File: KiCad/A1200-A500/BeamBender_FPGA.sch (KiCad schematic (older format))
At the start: 2 parts, among them U2 GW1NR-UV9LQ144P

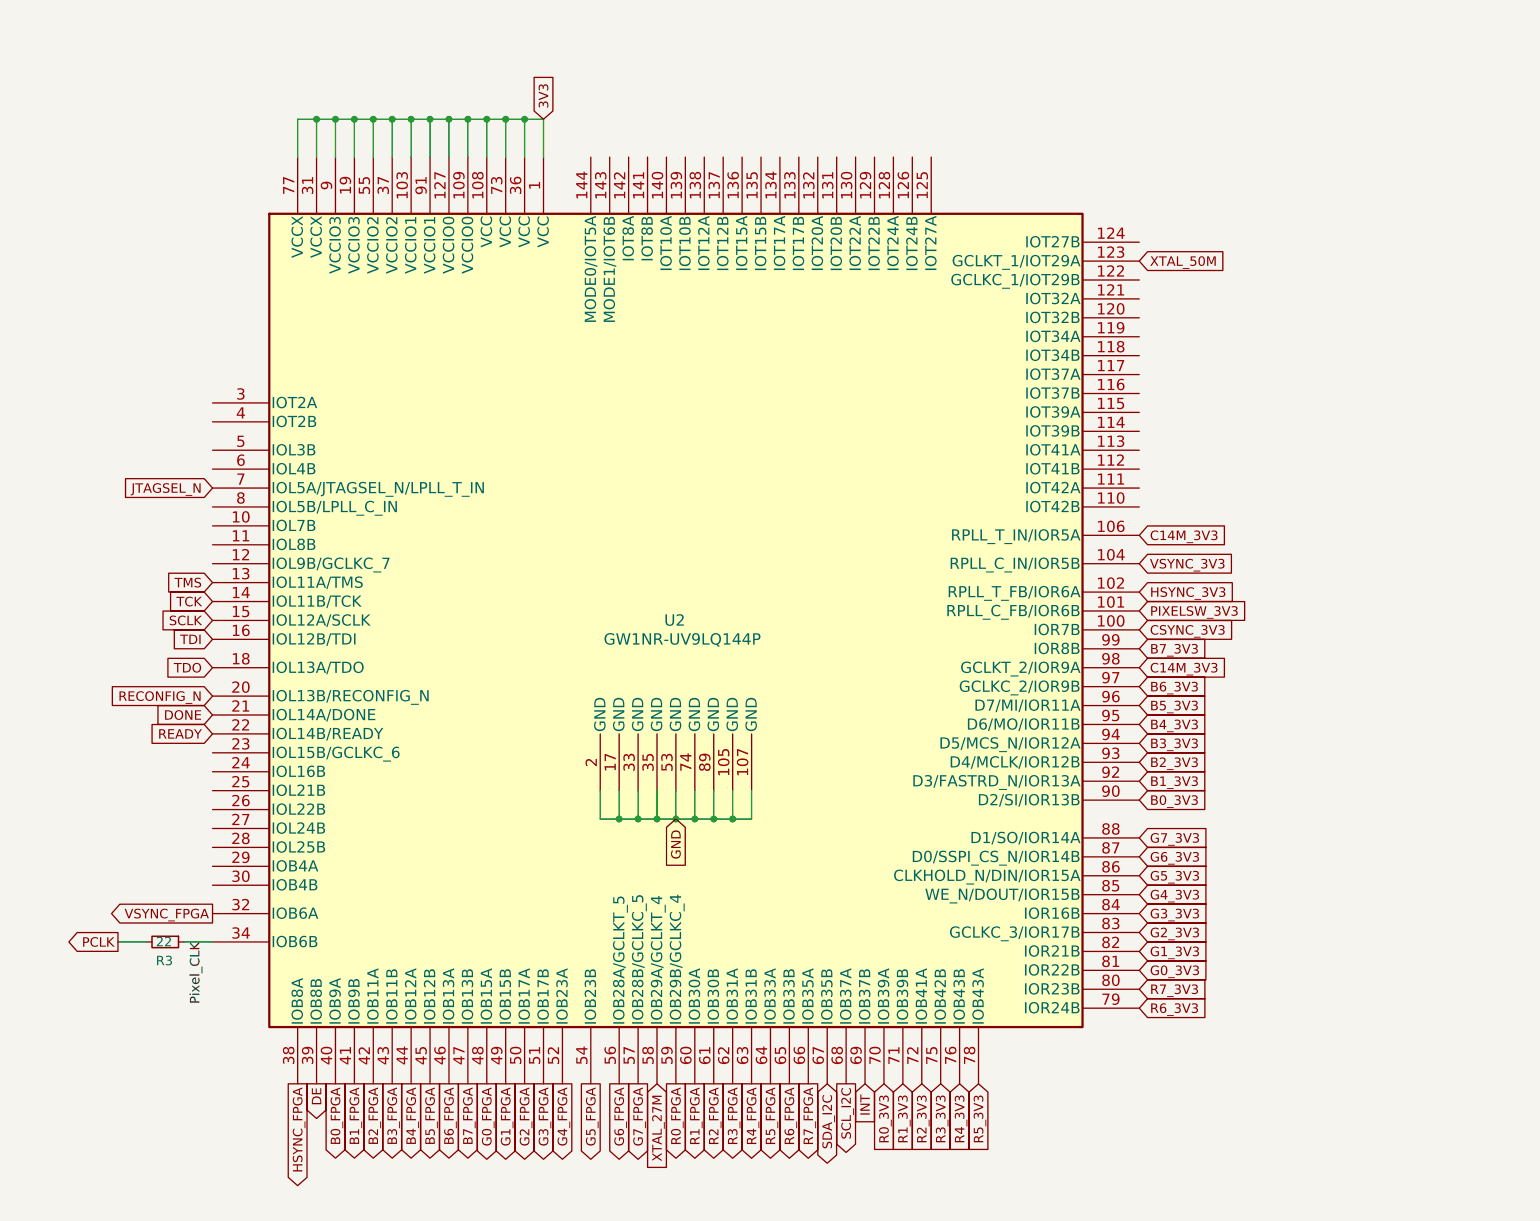
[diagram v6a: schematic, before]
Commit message: Breakout of own symbol for A500 drill-hole and more assignments of FPGA-pins
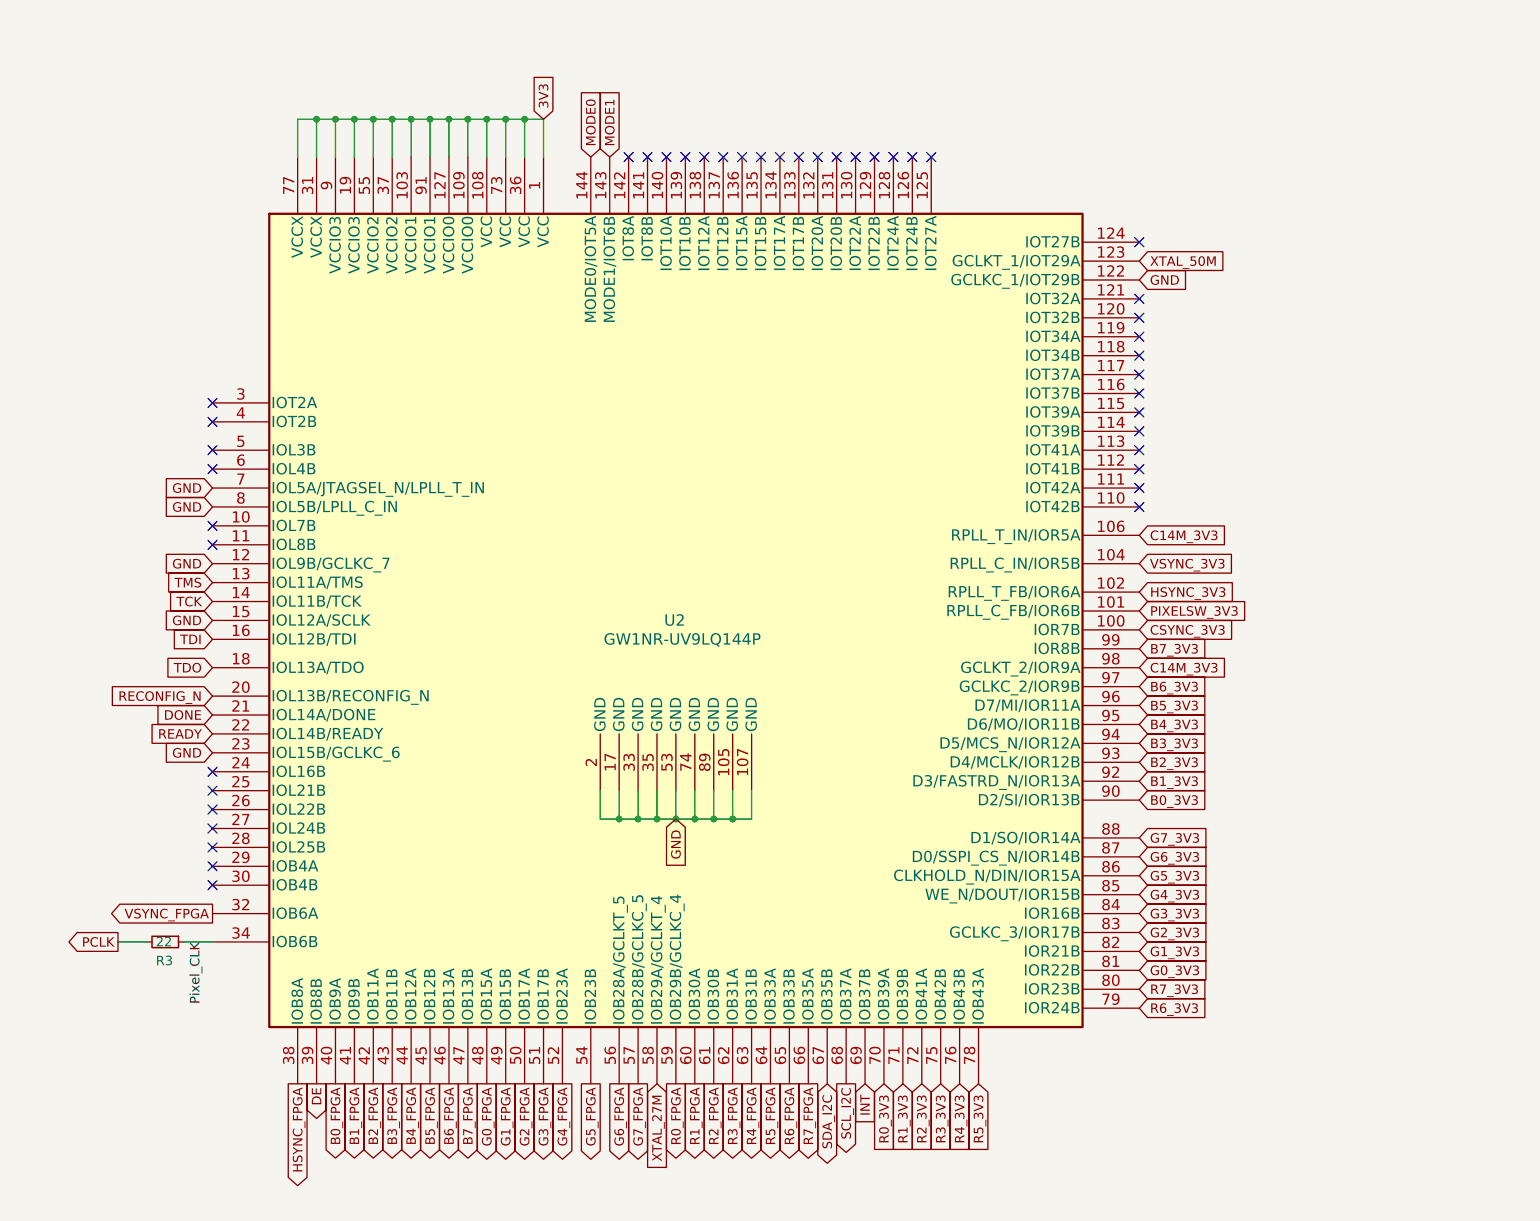
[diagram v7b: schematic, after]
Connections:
- net JTAGSEL_N is gone; now on net GND: U2.7 (IOL5A/JTAGSEL_N/LPLL_T_IN)
- net SCLK is gone; now on net GND: U2.15 (IOL12A/SCLK)
- net GND: now also U2.12 (IOL9B/GCLKC_7), U2.122 (GCLKC_1/IOT29B), U2.23 (IOL15B/GCLKC_6), U2.8 (IOL5B/LPLL_C_IN)
- net MODE1: now reaches U2.143 (MODE1/IOT6B)
- net MODE0: now reaches U2.144 (MODE0/IOT5A)
- no-connect marks 0 -> 43
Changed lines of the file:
@@
 Text GLabel 1600 3600 0    50   Input ~ 0
 TCK
-Text GLabel 1600 3700 0    50   Input ~ 0
-SCLK
 Text GLabel 1600 3800 0    50   Input ~ 0
 TDI
@@
 Text GLabel 1100 5400 0    50   Output ~ 0
 PCLK
-Text GLabel 1600 3000 0    50   Input ~ 0
-JTAGSEL_N
 Text GLabel 6500 3750 2    50   Input ~ 0
 CSYNC_3V3
@@
 Text Label 1550 5400 3    50   ~ 0
 Pixel_CLK
+Text GLabel 3600 1250 1    50   Input ~ 0
+MODE0
+Text GLabel 3700 1250 1    50   Input ~ 0
+MODE1
+Text GLabel 1600 3100 0    50   Input ~ 0
+GND
+Text GLabel 1600 3400 0    50   Input ~ 0
+GND
+Text GLabel 1600 3700 0    50   Input ~ 0
+GND
+Text GLabel 1600 4400 0    50   Input ~ 0
+GND
+Text GLabel 1600 3000 0    50   Input ~ 0
+GND
+NoConn ~ 1600 2550
+NoConn ~ 1600 2650
+NoConn ~ 1600 2800
+NoConn ~ 1600 2900
+NoConn ~ 1600 3200
+NoConn ~ 1600 3300
+NoConn ~ 1600 4500
+NoConn ~ 1600 4600
+NoConn ~ 1600 4700
+NoConn ~ 1600 4800
+NoConn ~ 1600 4900
+NoConn ~ 1600 5000
+NoConn ~ 1600 5100
+NoConn ~ 6500 1700
+NoConn ~ 6500 2000
+NoConn ~ 6500 2100
+NoConn ~ 6500 2200
+NoConn ~ 6500 2300
+NoConn ~ 6500 2400
+NoConn ~ 6500 2500
+NoConn ~ 6500 2600
+NoConn ~ 6500 2700
+NoConn ~ 6500 2800
+NoConn ~ 6500 2900
+NoConn ~ 6500 3000
+NoConn ~ 6500 3100
+NoConn ~ 3800 1250
+NoConn ~ 3900 1250
+NoConn ~ 4000 1250
+NoConn ~ 4100 1250
+NoConn ~ 4200 1250
+NoConn ~ 4300 1250
+NoConn ~ 4400 1250
+NoConn ~ 4500 1250
+NoConn ~ 4600 1250
+NoConn ~ 4700 1250
+NoConn ~ 4800 1250
+NoConn ~ 4900 1250
+NoConn ~ 5000 1250
+NoConn ~ 5100 1250
+NoConn ~ 5200 1250
+NoConn ~ 5300 1250
+NoConn ~ 5400 1250
+Text GLabel 6500 1900 2    50   Input ~ 0
+GND
 $EndSCHEMATC

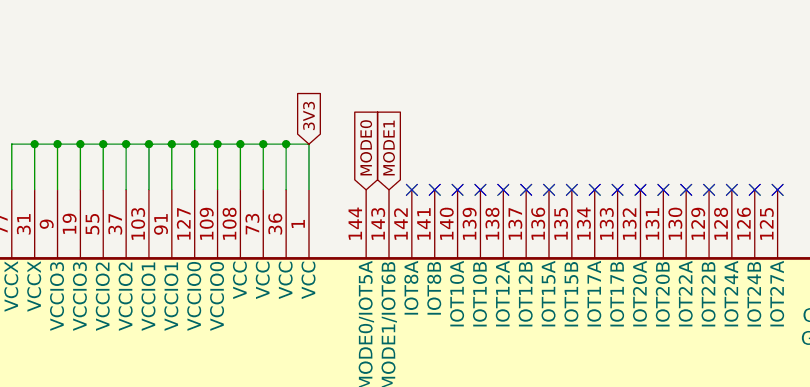
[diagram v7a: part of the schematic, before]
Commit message: Added 1k pull-down resistors on the FPGA's MODE0 and MODE1 pins
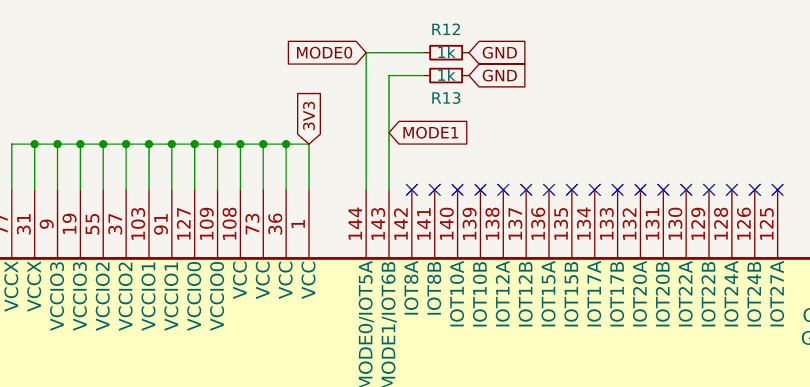
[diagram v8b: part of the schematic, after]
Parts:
- added R12, R13: 1k, Resistor_SMD:R_0805_2012Metric_Pad1.20x1.40mm_HandSolder, symbol Device:R_Small
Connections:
- net GND: now also R12.1, R13.1
- net MODE0: now also R12.2
- net MODE1: now also R13.2
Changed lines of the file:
@@
 Text Label 1550 5400 3    50   ~ 0
 Pixel_CLK
-Text GLabel 3600 1250 1    50   Input ~ 0
+Text GLabel 3600 650  0    50   Input ~ 0
 MODE0
-Text GLabel 3700 1250 1    50   Input ~ 0
+Text GLabel 3700 1000 2    50   Input ~ 0
 MODE1
 Text GLabel 1600 3100 0    50   Input ~ 0
@@
 Text GLabel 6500 1900 2    50   Input ~ 0
 GND
+$Comp
+L Device:R_Small R13
+U 1 1 661C34A6
+P 3950 750
+F 0 "R13" V 4050 750 50  0000 C CNN
+F 1 "1k" V 3950 750 50  0000 C CNN
+F 2 "Resistor_SMD:R_0805_2012Metric_Pad1.20x1.40mm_HandSolder" H 3950 750 50  0001 C CNN
+F 3 "~" H 3950 750 50  0001 C CNN
+	1    3950 750
+	0    1    1    0
+$EndComp
+$Comp
+L Device:R_Small R12
+U 1 1 661D4C0B
+P 3950 650
+F 0 "R12" V 3850 650 50  0000 C CNN
+F 1 "1k" V 3950 650 50  0000 C CNN
+F 2 "Resistor_SMD:R_0805_2012Metric_Pad1.20x1.40mm_HandSolder" H 3950 650 50  0001 C CNN
+F 3 "~" H 3950 650 50  0001 C CNN
+	1    3950 650
+	0    1    1    0
+$EndComp
+Wire Wire Line
+	3600 1250 3600 650
+Wire Wire Line
+	3600 650  3850 650
+Wire Wire Line
+	3700 1250 3700 750
+Wire Wire Line
+	3700 750  3850 750
+Text GLabel 4050 650  2    50   Input ~ 0
+GND
+Text GLabel 4050 750  2    50   Input ~ 0
+GND
 $EndSCHEMATC
